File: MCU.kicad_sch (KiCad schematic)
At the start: 27 parts, among them J2 AVR-ISP-6, J3 USB_B, J7 Screw, U3 ATmega2560-16A, Y1 16MHz

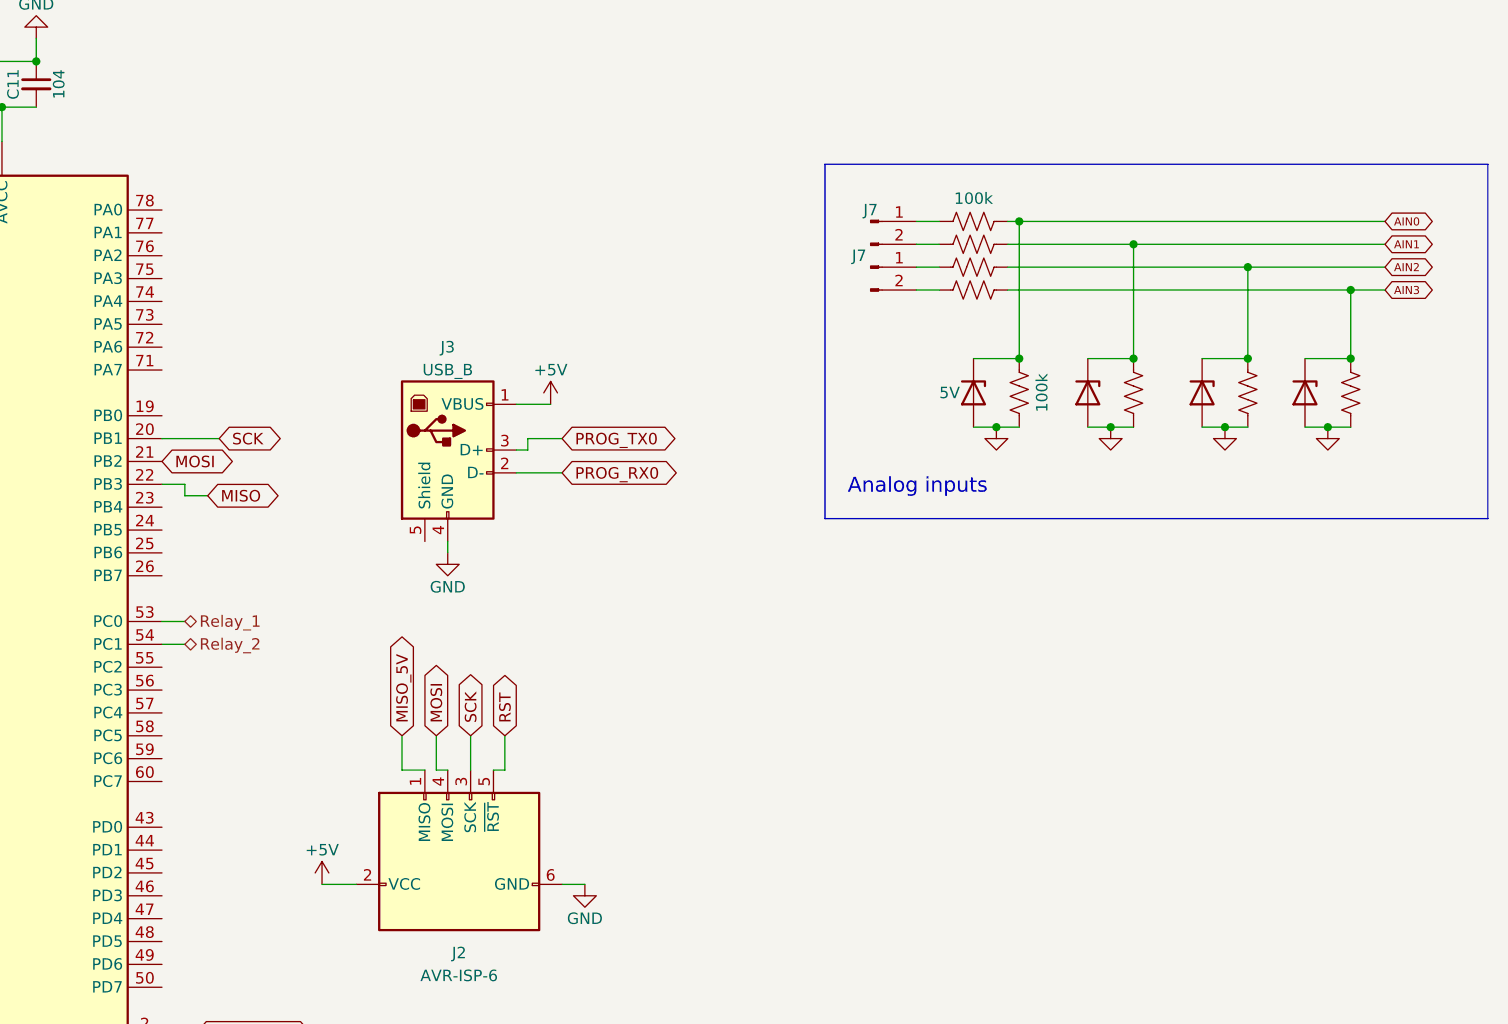
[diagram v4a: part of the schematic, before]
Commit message: Schematic of 4-20mA sensor
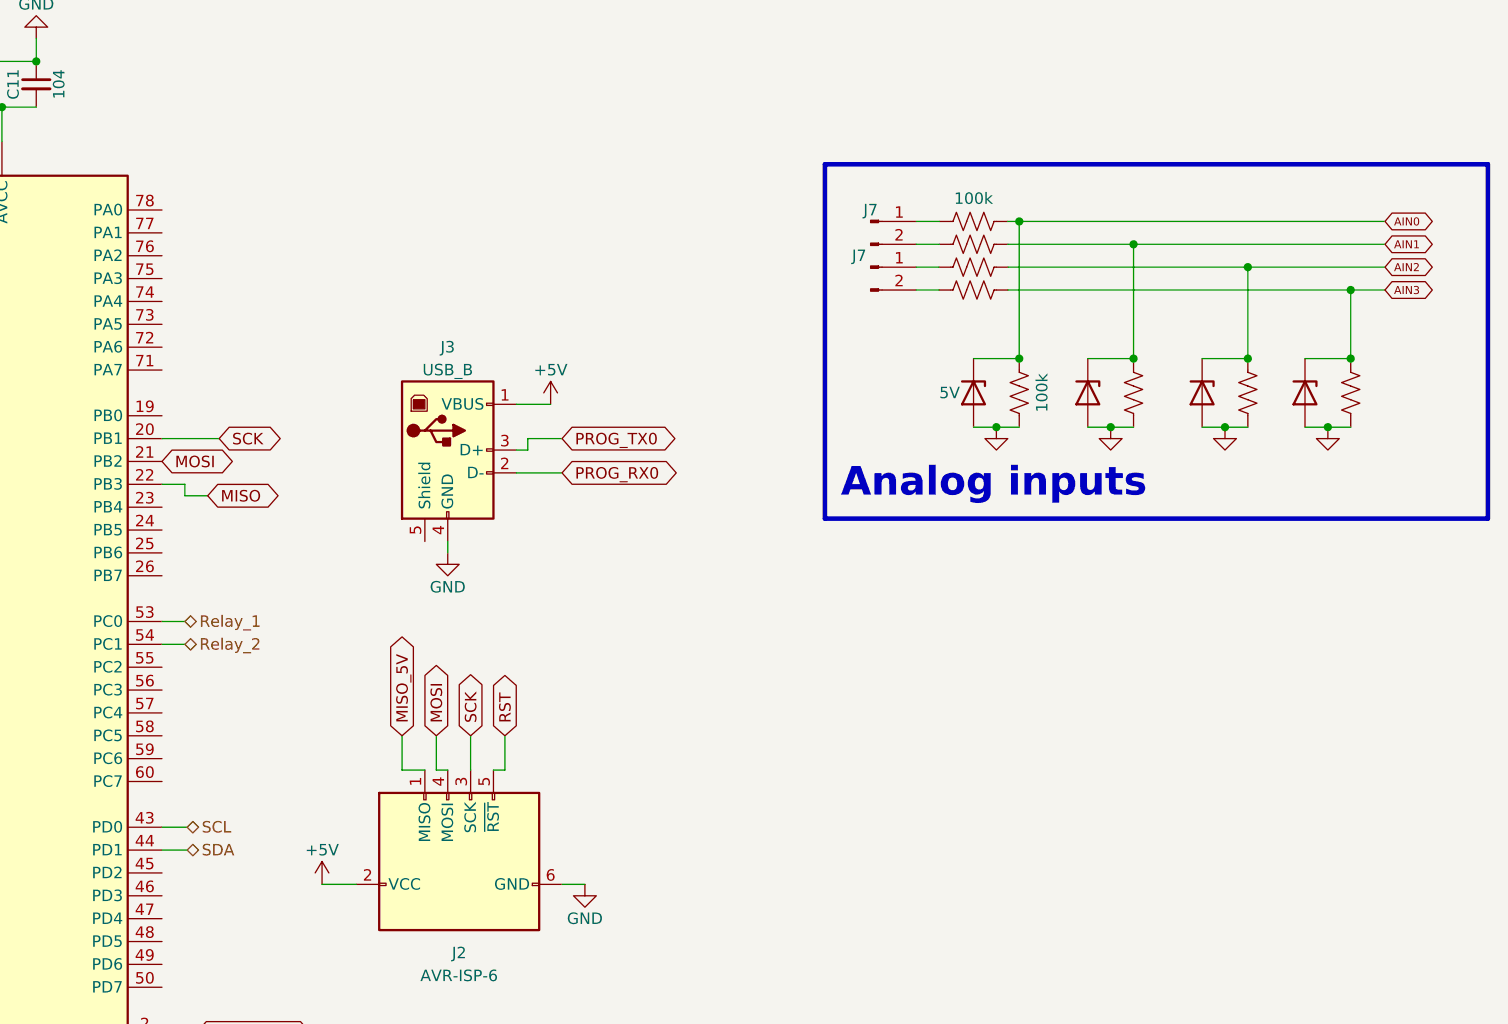
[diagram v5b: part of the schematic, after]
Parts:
- R23: footprint (none) -> Resistor_SMD:R_1206_3216Metric
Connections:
- net SCL: now reaches U3.43 (PD0)
- net SDA: now reaches U3.44 (PD1)
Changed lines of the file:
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@@
+    (stroke (width 0) (type default))
+  )
+  (wire (pts (xy 114.554 111.76) (xy 111.76 111.76))
     (stroke (width 0) (type default))
   )
@@
     (stroke (width 0) (type default))
   )
+  (wire (pts (xy 114.554 114.3) (xy 111.76 114.3))
+    (stroke (width 0) (type default))
+  )
   (wire (pts (xy 156.21 118.11) (xy 158.75 118.11))
     (stroke (width 0) (type default))
@@
   )
   (rectangle (start 185.42 38.1) (end 259.08 77.47)
-    (stroke (width 0) (type default))
+    (stroke (width 0.508) (type default))
     (fill (type none))
   )
-  (text "Analog inputs" (at 187.96 74.93 0)
-    (effects (font (size 1.651 1.651)) (justify left bottom))
+  (text "Analog inputs" (at 187.198 75.438 0)
+    (effects (font (size 3.175 3.175) (thickness 0.635) bold) (justify left bottom))
   )
   (global_label "AIN0" (shape bidirectional) (at 66.04 88.9 180) (fields_autoplaced)
@@
     )
   )
+  (hierarchical_label "SCL" (shape bidirectional) (at 114.554 111.76 0) (fields_autoplaced)
+    (effects (font (size 1.27 1.27)) (justify left))
+  )
   (hierarchical_label "DIN2" (shape bidirectional) (at 63.5 121.92 180) (fields_autoplaced)
     (effects (font (size 1.27 1.27)) (justify right))
@@
   (hierarchical_label "GND" (shape bidirectional) (at 91.44 184.15 180) (fields_autoplaced)
     (effects (font (size 1.27 1.27)) (justify right))
+  )
+  (hierarchical_label "SDA" (shape bidirectional) (at 114.554 114.3 0) (fields_autoplaced)
+    (effects (font (size 1.27 1.27)) (justify left))
   )
   (hierarchical_label "DIN3" (shape bidirectional) (at 63.5 124.46 180) (fields_autoplaced)
@@
       (effects (font (size 1.27 1.27)))
     )
-    (property "Footprint" "" (at 202.184 43.434 90)
-      (effects (font (size 1.27 1.27)) hide)
-    )
+    (property "Footprint" "Resistor_SMD:R_1206_3216Metric" (at 202.184 43.434 90)
+      (effects (font (size 1.27 1.27)) hide)
+    )
